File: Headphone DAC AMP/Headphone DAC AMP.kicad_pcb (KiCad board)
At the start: 2 copper layers, 157 parts, among them J4 PINHD_1x2_Male, J5 PINHD_2x3_Male, U6 MCP1727-1802xSN, U7 MCP1727-3302xSN, U9 TPS717XX, Y1 Crystal_GND24, Y2 LMK6CE049152CDLFR, Y3 ASDLJ-E-45.1584MHz

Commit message: test
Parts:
- moved C5 5.69 mm to (100.0, 47.2)
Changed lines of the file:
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@@
 	(footprint "Capacitor_SMD:C_0805_2012Metric_Pad1.18x1.45mm_HandSolder"
 		(layer "F.Cu")
-		(at 105.65 47.24)
+		(at 99.9625 47.225)
 		(descr "Capacitor SMD 0805 (2012 Metric), square (rectangular) end terminal, IPC-7351 nominal with elongated pad for handsoldering. (Body size source: IPC-SM-782 page 76, https://www.pcb-3d.com/wordpress/wp-content/uploads/ipc-sm-782a_amendment_1_and_2.pdf, https://docs.google.com/spreadsheets/d/1BsfQQcO9C6DZCsRaXUlFlo91Tg2WpOkGARC1WS5S8t0/edit?usp=sharing), generated with kicad-footprint-generator")
 		(tags "capacitor handsolder")

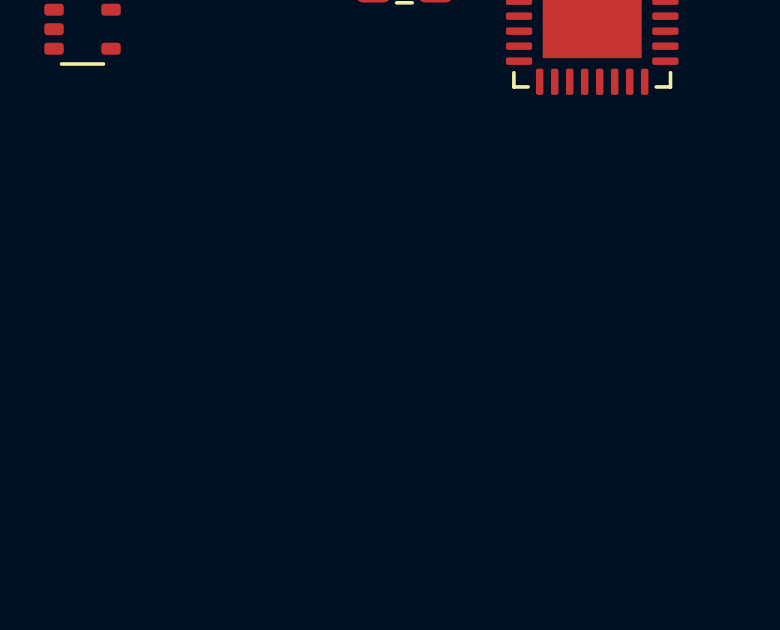
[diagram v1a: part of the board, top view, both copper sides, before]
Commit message: uPDATED fOOTPRINTS
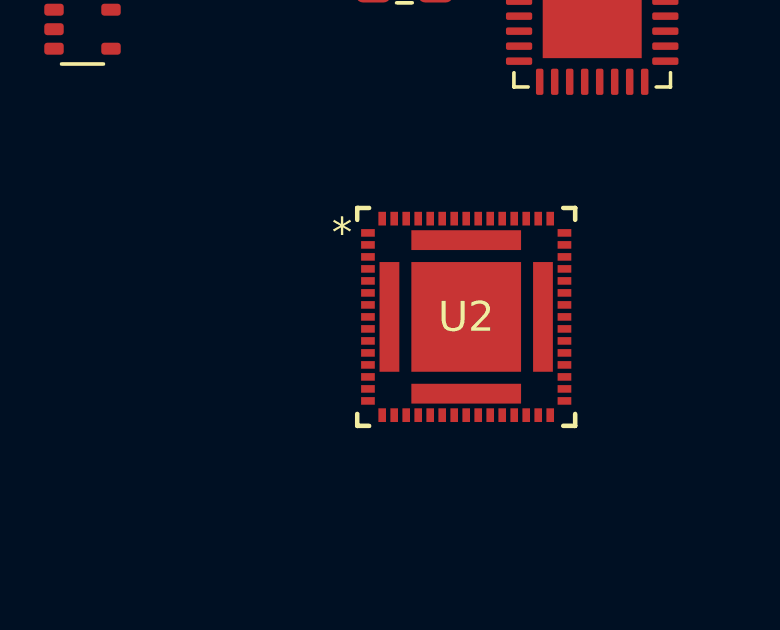
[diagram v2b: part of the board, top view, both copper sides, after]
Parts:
- added U2: XU316-1024-QF60B-C24, footprints:QFN_F60B-C24_XMO, F.Cu at (153.7, 99.6)

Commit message: uPDATED MORE FOOTPRINTS
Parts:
- added C100: 100n, Capacitor_SMD:C_0402_1005Metric_Pad0.74x0.62mm_HandSolder, F.Cu at (158.6, 114.4)
- added C101: 100n, Capacitor_SMD:C_0402_1005Metric_Pad0.74x0.62mm_HandSolder, F.Cu at (158.6, 116.4)
- added C102: 100n, Capacitor_SMD:C_0402_1005Metric_Pad0.74x0.62mm_HandSolder, F.Cu at (158.6, 118.4)
- added C103: 100n, Capacitor_SMD:C_0402_1005Metric_Pad0.74x0.62mm_HandSolder, F.Cu at (158.6, 120.3)
- added F1: 2A, Fuse:Fuse_0805_2012Metric_Pad1.15x1.40mm_HandSolder, F.Cu at (197.2, 84.3)
- added J1: 2137160001, 2137160001:MOLEX_2137160001, F.Cu at (185.0, 91.5)
- added J2: M50-3551042, M50_3551042:HARWIN_M50-3551042, F.Cu at (95.5, 155.5)
- added U11: ADP5071AREZ-R7, ADP5071:RE-20-1_ADI, F.Cu at (73.1, 67.8)
- added U12: TPS74501PDRVR, TPS74501PDRVR:SON65P200X200X80-7N, F.Cu at (70.7, 74.0)
- added U14: ADP7185ACPZN-R7, ADP7185ACPZN-R7:SON50P200X200X60-9N, F.Cu at (74.9, 74.0)
- added U4: OPA1612AxD, Package_SO:SOIC-8-1EP_3.9x4.9mm_P1.27mm_EP2.95x4.9mm_Mask2.71x3.4mm_ThermalVias, F.Cu at (136.5, 105.4)
- added U5: OPA1612AxD, Package_SO:SOIC-8-1EP_3.9x4.9mm_P1.27mm_EP2.95x4.9mm_Mask2.71x3.4mm_ThermalVias, F.Cu at (136.5, 111.9)
- C1, C2, C3, C4, C40, C95: value 1uF -> 1u
- C10, C11, C12, C13, C14, C15, C16, C17, C9, C96, C97, C98, C99: value 100nf -> 100n; footprint Capacitor_SMD:C_0805_2012Metric_Pad1.18x1.45mm_HandSolder -> Capacitor_SMD:C_0402_1005Metric_Pad0.74x0.62mm_HandSolder
- C18, C19, C23, C24: value 100nF -> 100n; footprint Capacitor_SMD:C_0805_2012Metric_Pad1.18x1.45mm_HandSolder -> Capacitor_SMD:C_0402_1005Metric_Pad0.74x0.62mm_HandSolder
- C22, C39, C56, C59, C60, C63, C64, C67, C68, C69, C70, C73, C74, C75, C78, C79, C80, C83, C84, C85, C86, C87, C88, C89, C90, C91, C92, C93, C94: footprint Capacitor_SMD:C_0805_2012Metric_Pad1.18x1.45mm_HandSolder -> Capacitor_SMD:C_0402_1005Metric_Pad0.74x0.62mm_HandSolder
- U1: value ~ -> ES9039Q2M
- moved C64 146.2 mm to (229.7, 143.9)
- moved C75 139.4 mm to (233.4, 139.4)
- moved C74 139.4 mm to (233.4, 136.3)
- moved C80 114.9 mm to (193.8, 141.3)
- moved C89 114.9 mm to (198.7, 141.3)
- moved C69 114.6 mm to (190.5, 133.7)
- moved C70 114.6 mm to (190.5, 136.7)
- moved C78 114.6 mm to (195.3, 133.7)
- moved C79 114.6 mm to (195.3, 136.7)
- moved C87 114.6 mm to (200.1, 133.7)
- moved C88 114.6 mm to (200.1, 136.7)
- moved C92 111.0 mm to (207.0, 137.0)
- moved C93 111.0 mm to (207.0, 140.0)
- moved C90 111.0 mm to (207.0, 131.0)
- moved C91 111.0 mm to (207.0, 134.0)
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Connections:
- C59 pad 1: +3V3 -> +3.3V
- C60 pad 1: +1V8 -> +1.8V
- R40 pad 1: +1V8 -> +1.8V

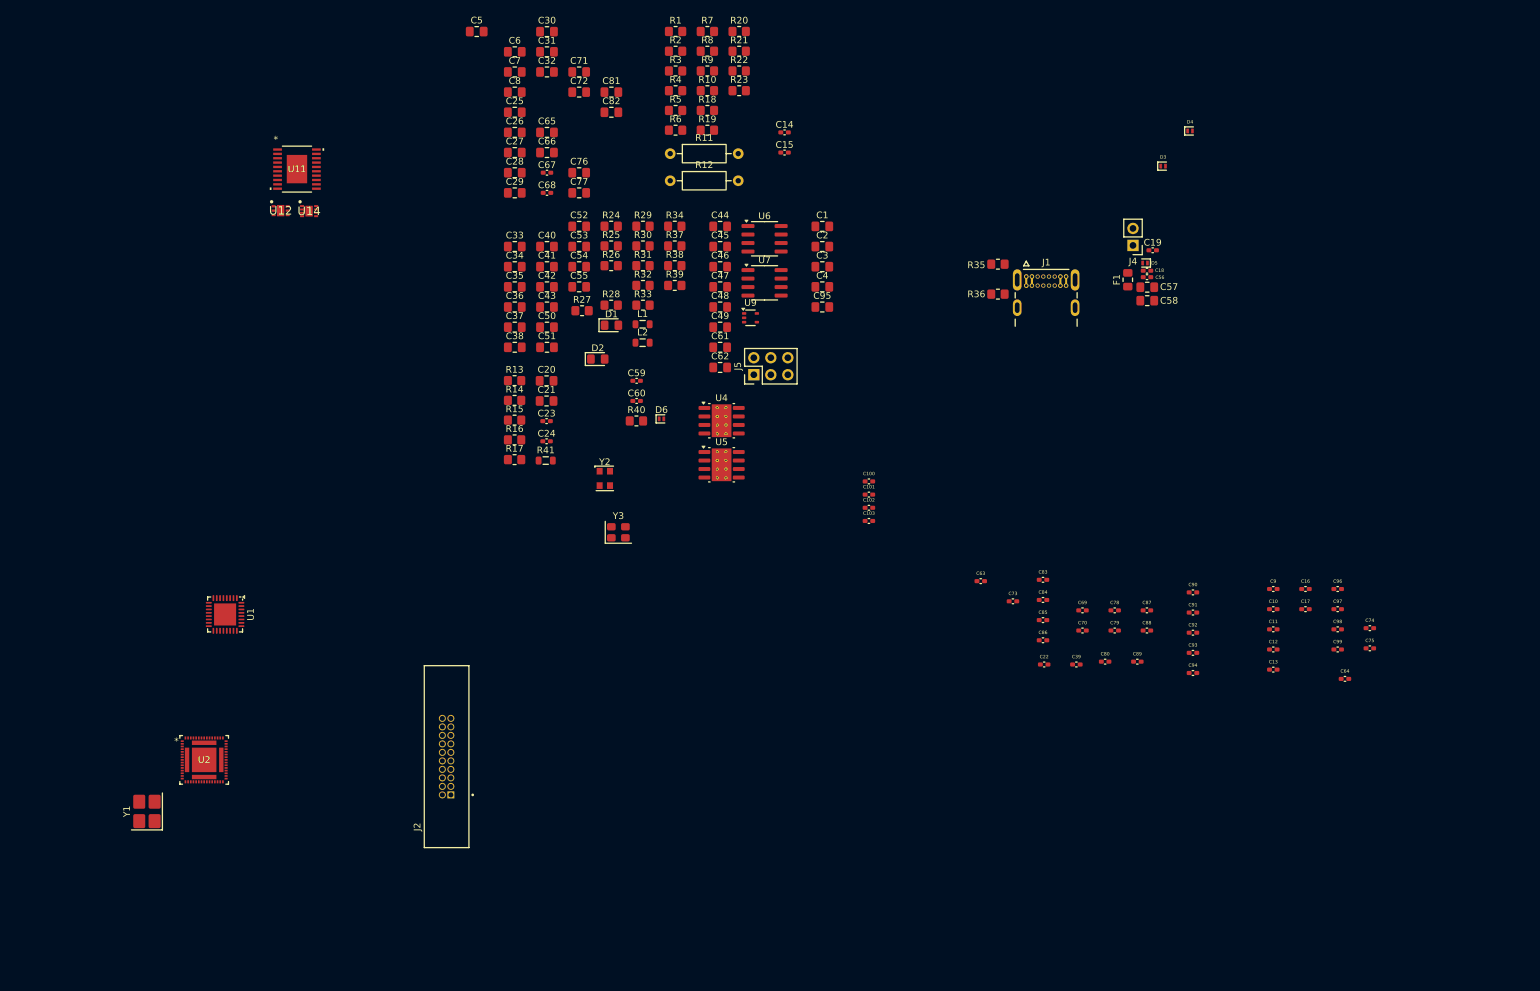
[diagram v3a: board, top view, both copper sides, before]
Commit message: Added PCB Filtering
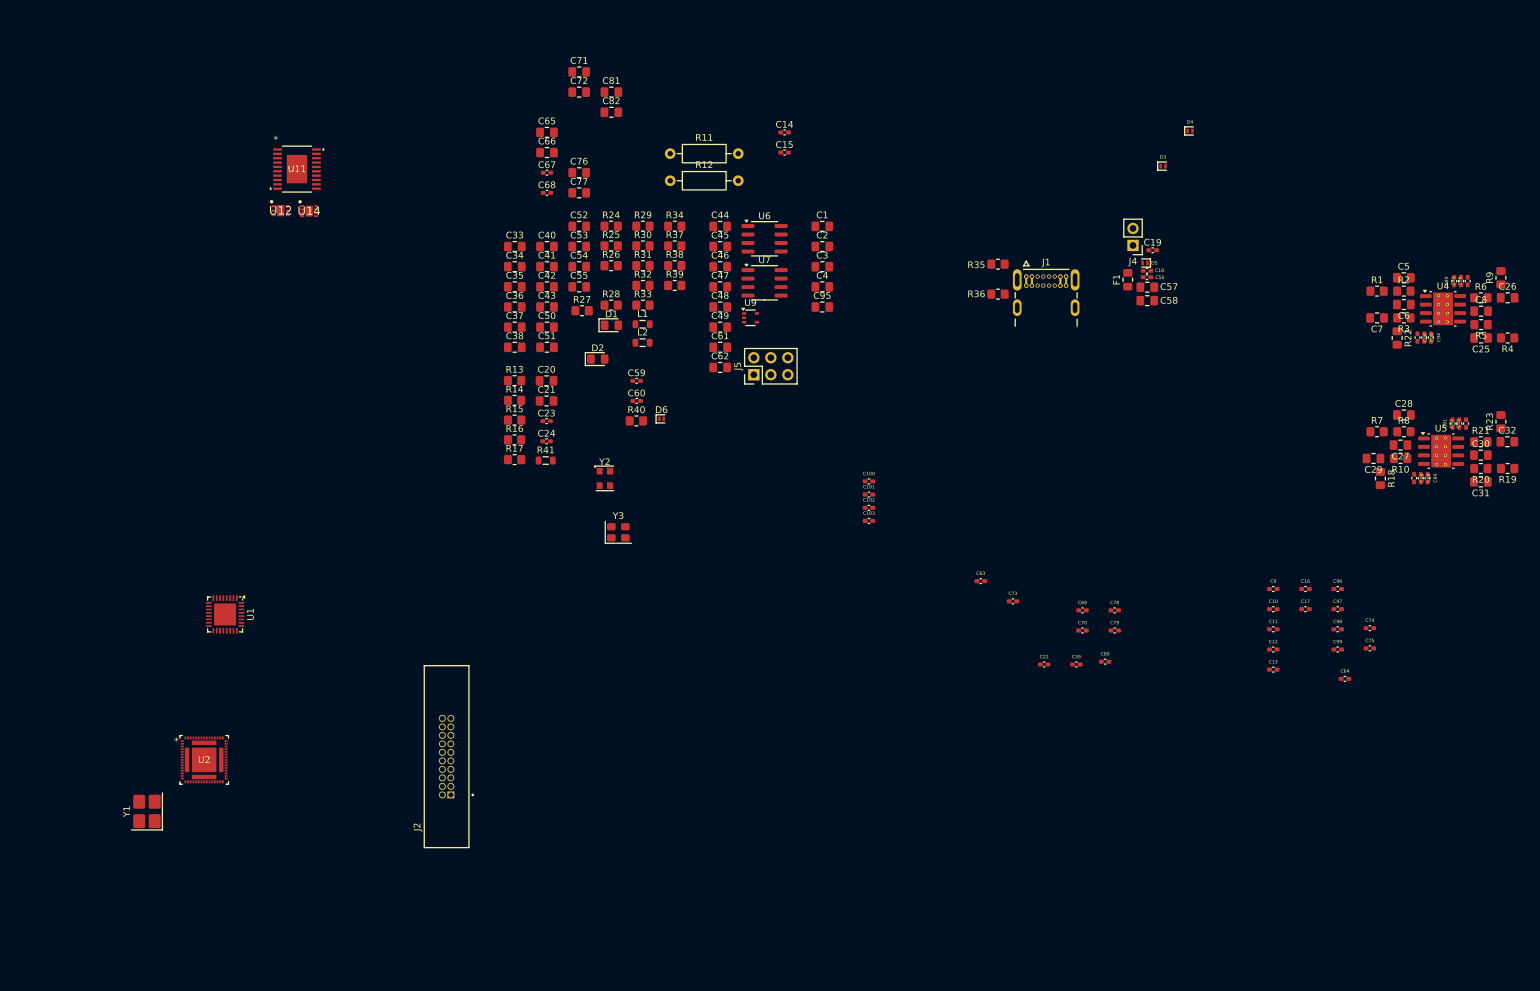
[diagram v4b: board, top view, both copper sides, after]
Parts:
- moved C32 153.7 mm to (253.9, 108.5)
- moved C31 153.6 mm to (250.0, 114.5), turned to 180 degrees
- moved C30 153.2 mm to (250.0, 110.5)
- moved C26 150.4 mm to (254.0, 87.0)
- moved C25 148.2 mm to (250.0, 93.0), turned to 180 degrees
- moved C8 148.0 mm to (250.0, 89.0)
- moved C5 143.3 mm to (238.5, 84.0)
- moved C27 139.3 mm to (238.0, 109.0), turned to 180 degrees
- moved C6 138.1 mm to (238.5, 88.0), turned to 180 degrees
- moved C28 137.7 mm to (238.5, 104.5)
- moved C29 134.3 mm to (233.9, 111.0), turned to 180 degrees
- moved C7 133.9 mm to (234.5, 90.0), turned to 180 degrees
- moved R19 129.8 mm to (254.0, 112.5), turned to 180 degrees
- moved R4 129.7 mm to (254.0, 93.0), turned to 180 degrees
- moved R20 128.6 mm to (250.0, 112.5), turned to 180 degrees
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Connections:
- U4 pad 4: /Headphone Amp Stage/L+FLT -> /Headphone Amp Stage/L-FLT
- U5 pad 8: /Headphone Amp Stage/L-FLT -> /Headphone Amp Stage/L+FLT

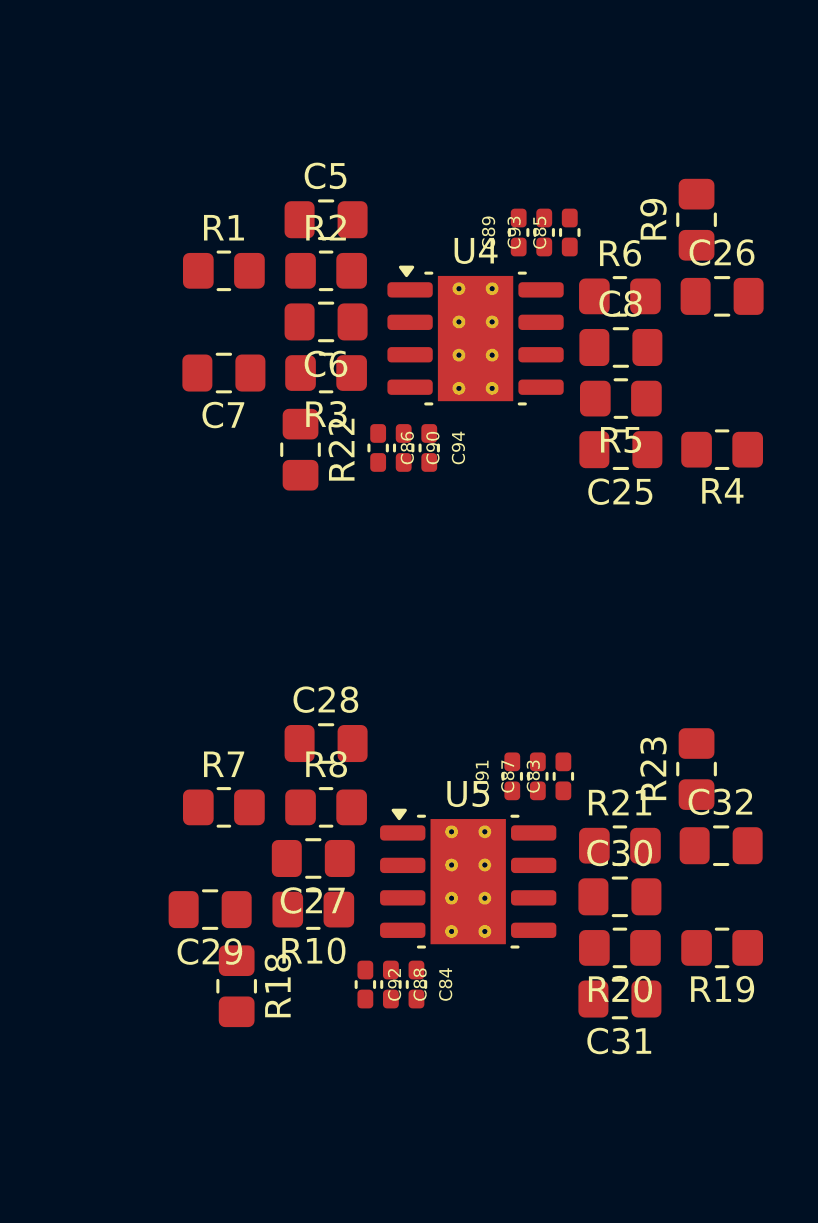
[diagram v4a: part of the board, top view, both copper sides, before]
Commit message: Added filtering to PCB
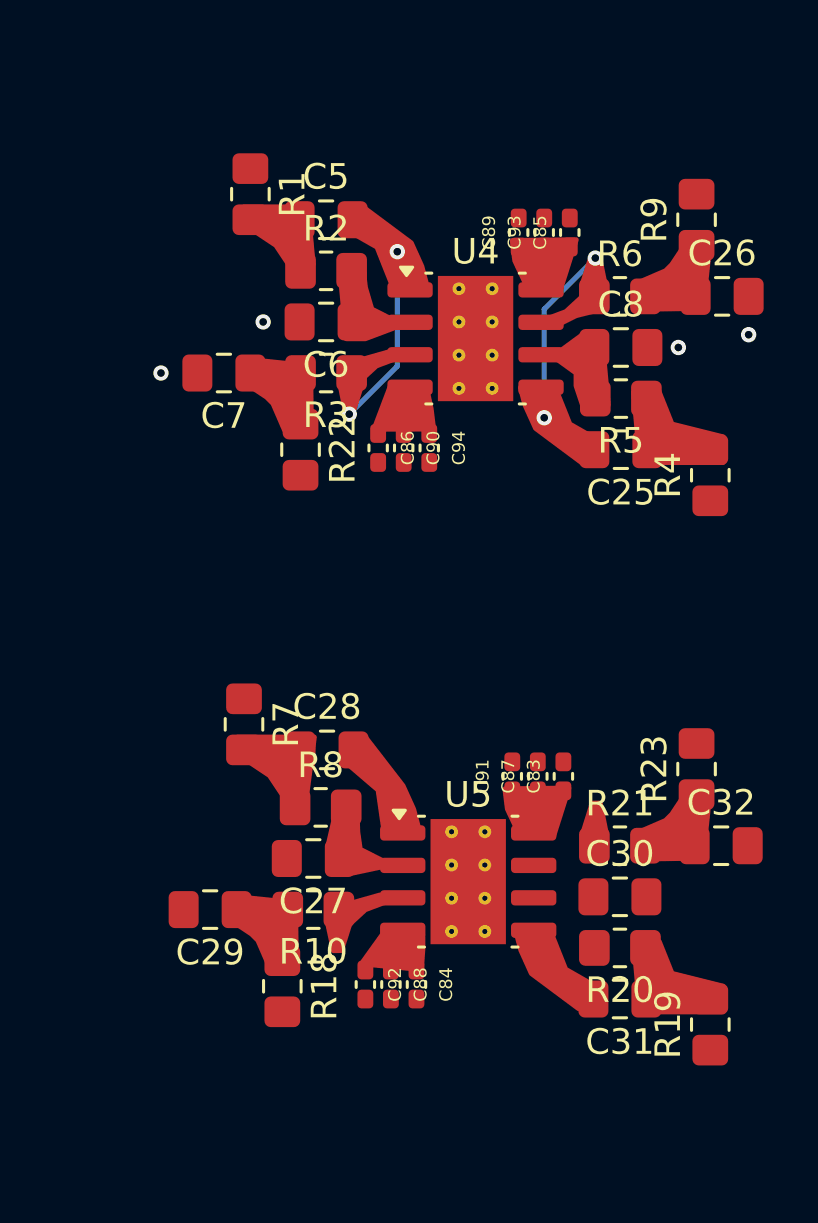
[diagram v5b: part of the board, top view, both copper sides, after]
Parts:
- moved R7 3.34 mm to (235.2, 103.8), turned to -90 degrees
- moved R1 3.17 mm to (235.5, 83.0), turned to -90 degrees
- moved R19 3.04 mm to (253.5, 115.5), turned to 90 degrees
- moved R18 1.79 mm to (236.8, 114.0)
- moved R4 1.10 mm to (253.5, 94.0), turned to 90 degrees
- moved C28 0.25 mm to (238.5, 104.8)
- moved R8 0.21 mm to (238.2, 107.0)
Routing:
- net Net-(U4A-+): track 0.00 -> 7.14 mm, vias 0 -> 2
- net Net-(U4B-+): track 0.00 -> 7.08 mm, vias 0 -> 2
- net Net-(U4B--): track 0.00 -> 0.51 mm
- net GND: vias 0 -> 1
- net (no net): vias 0 -> 3

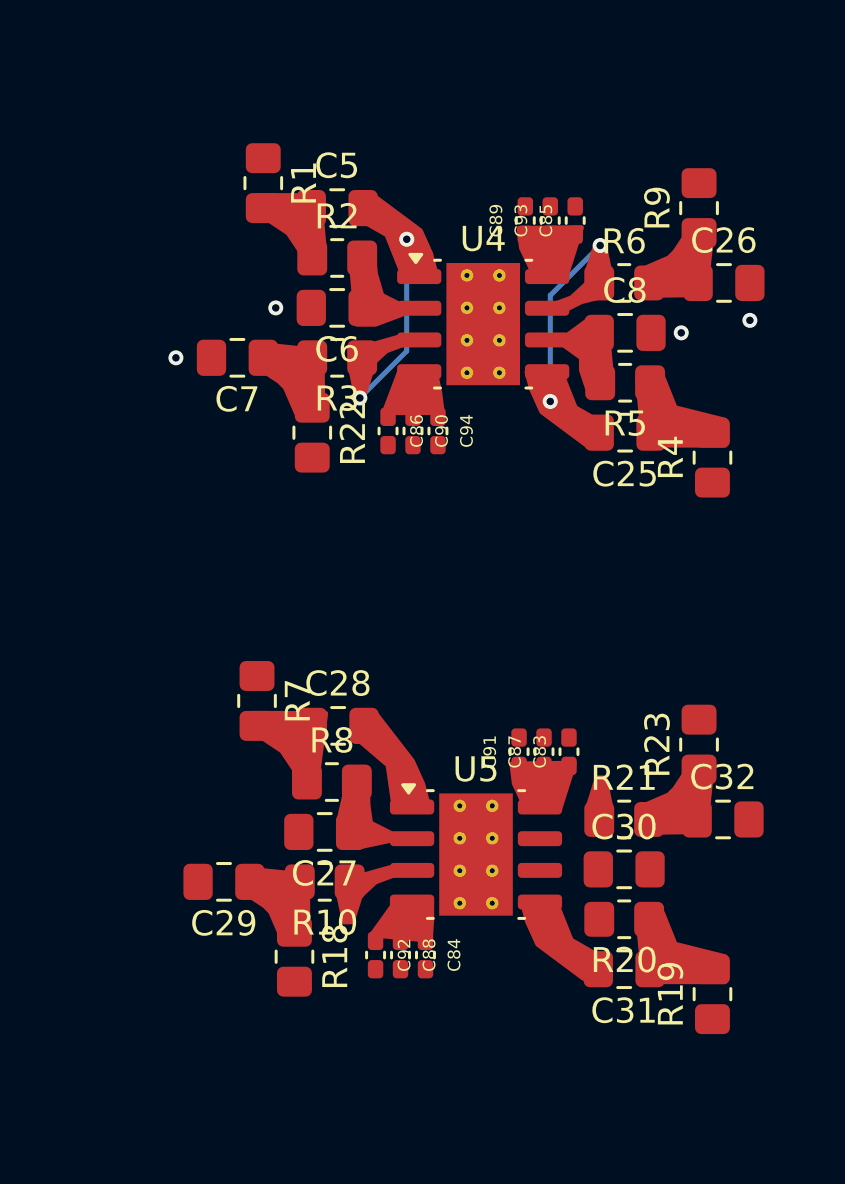
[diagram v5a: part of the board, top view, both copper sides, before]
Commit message: added filtering ground
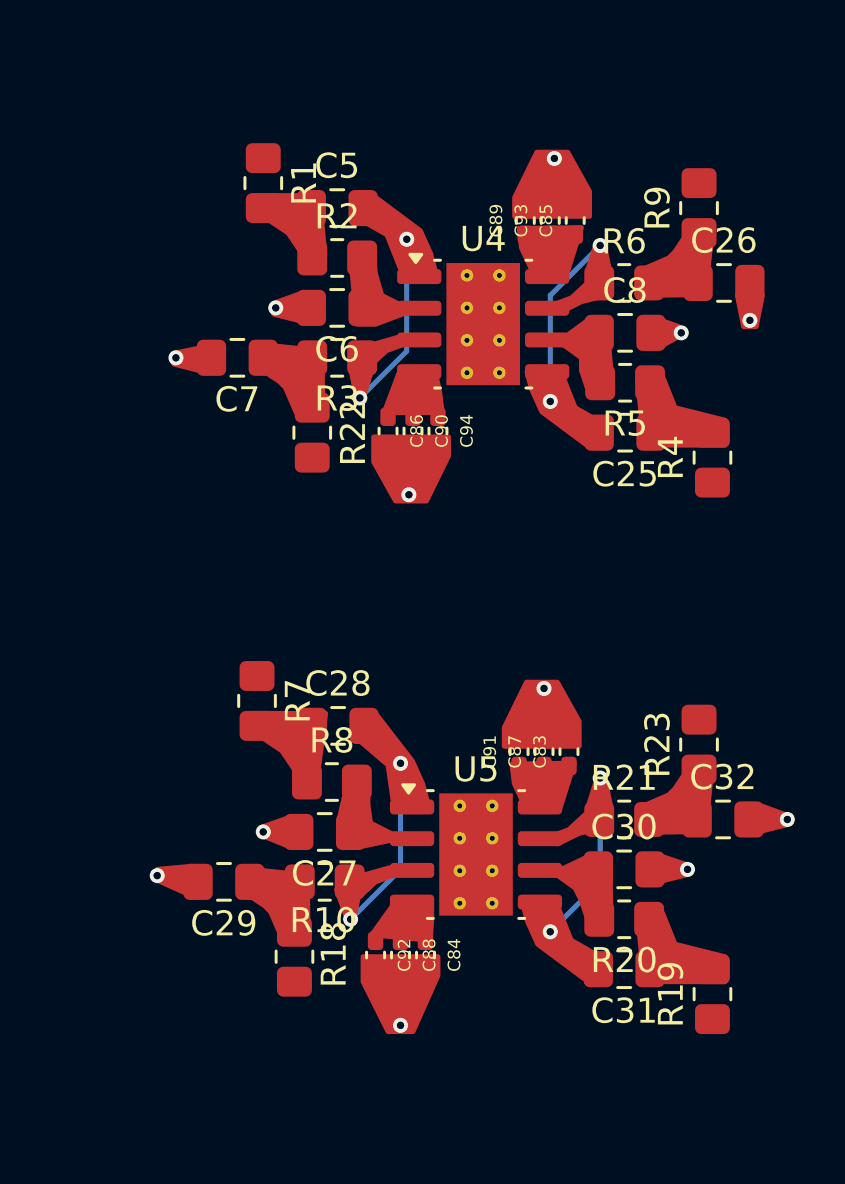
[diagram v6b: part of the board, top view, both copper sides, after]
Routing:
- net Net-(U5A-+): track 0.00 -> 7.08 mm, vias 0 -> 2
- net Net-(U5B-+): track 0.00 -> 6.99 mm, vias 0 -> 2
- net GND: vias 1 -> 12
- net (no net): vias 3 -> 0
